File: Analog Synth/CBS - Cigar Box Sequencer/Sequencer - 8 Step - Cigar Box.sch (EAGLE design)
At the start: 204 parts, among them IC1 TL084P, IC10 79L05, IC11 MCP6002, IC12 74AC138N, IC13 74ALS04N, IC14 74AC138N, IC15 74ALS04N, IC16 74ALS04N, IC17 74ALS08N, IC2 TL084P, IC3 TL084P, IC4 74ALS04N, IC5 4050N, IC6 78L05, IC7 74HC193N, IC8 78L05, IC9 74LS86N, Q1 I/O, Q14 J310, Q15 J310, Q16 J310, Q17 J310, Q18 J310, Q19 J310, Q2 I/O, Q20 J310, Q3 I/O, Q4 2N3906, Q5 2N3904, Q6 J310, X1 I/O, X2 I/O, X3 I/O

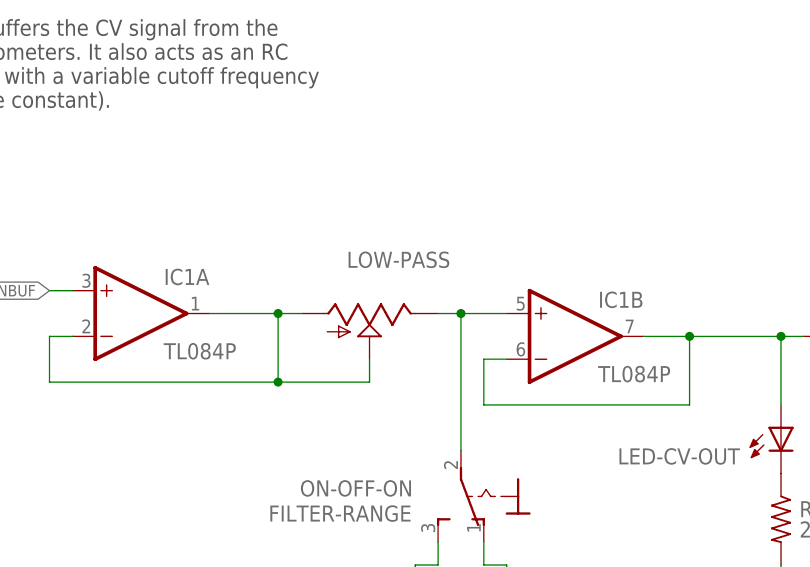
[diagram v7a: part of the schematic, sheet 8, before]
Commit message: CBS: fixed missing potentiometer value for output CV filter
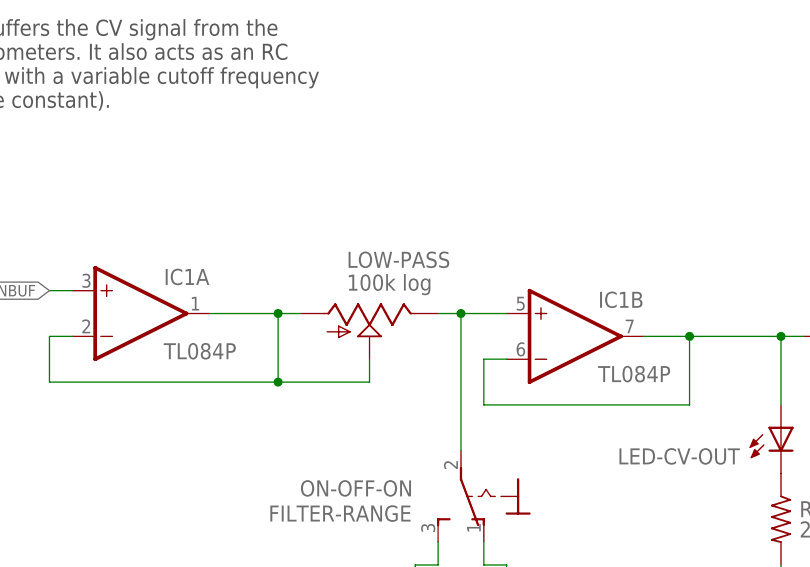
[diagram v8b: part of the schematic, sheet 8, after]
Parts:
- LOW-PASS: value (none) -> 100k log
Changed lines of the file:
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@@
 <part name="SUPPLY36" library="supply2" deviceset="GND" device=""/>
 <part name="IC1" library="linear" deviceset="TL084" device="P"/>
-<part name="LOW-PASS" library="pot" deviceset="TRIM_US-" device="B64Y"/>
+<part name="LOW-PASS" library="pot" deviceset="TRIM_US-" device="B64Y" value="100k log"/>
 <part name="LED-CV-OUT" library="led" deviceset="TLLG4400" device="" value=""/>
 <part name="FILTER-RANGE" library="switch" deviceset="320-916" device="" value="ON-OFF-ON"/>
